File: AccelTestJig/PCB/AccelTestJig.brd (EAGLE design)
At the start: 10.2 x 24.1 mm, 11 parts, among them Q1 MMBTA56-SOT23, U1 MMA8653FCR1

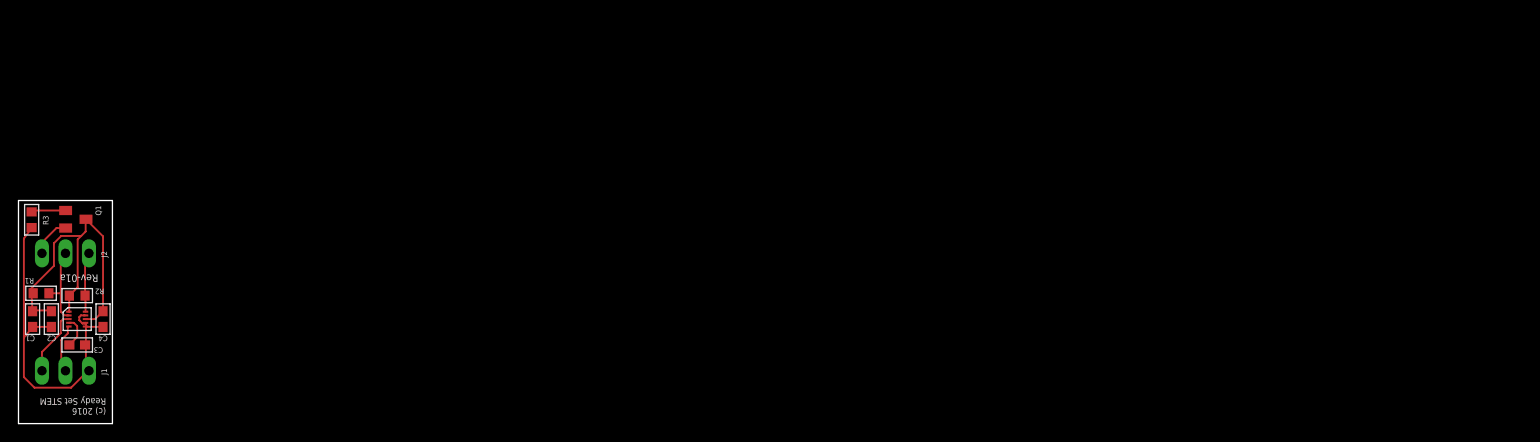
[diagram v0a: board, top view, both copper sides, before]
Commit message: AccelTestJig - first rev (sent to oshpark)
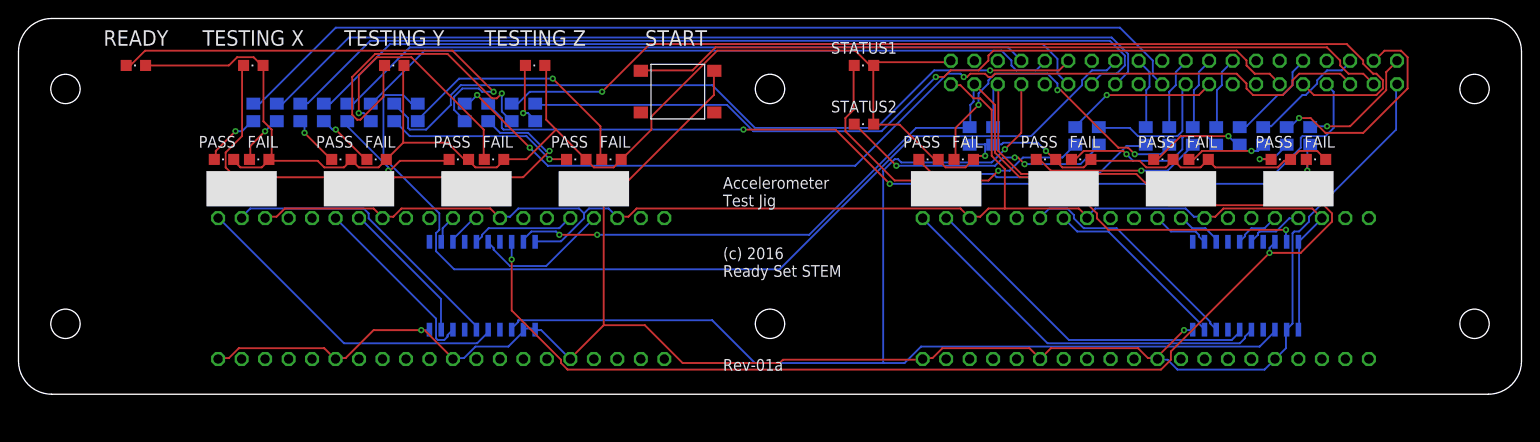
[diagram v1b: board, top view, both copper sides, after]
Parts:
- removed C1, C3, C4: 0.1uF, AccelBreakout:C0603
- removed C2: 1uF, AccelBreakout:C0603
- removed J1, J2: (no value), AccelBreakout:1X03
- removed Q1: MMBTA56-SOT23, transistor-pnp:SOT23
- added FAIL0, FAIL1, FAIL2, FAIL3, FAIL4, FAIL5, FAIL6, FAIL7: FAIL, led:CHIPLED_0805
- added JP1: NONE, AccelTestJig:2X20
- added JP2, JP3: NONE, AccelTestJig:2X20-WIDE
- added PASS0, PASS1, PASS2, PASS3, PASS4, PASS5, PASS6, PASS7: PASS, led:CHIPLED_0805
- added R10, R11, R12, R13, R14, R15, R16, R17, R18, R19, R20, R21, R22, R4, R5, R6, R7, R8, R9: 100, resistor:R0805
- added R23, R24: 10k, resistor:R0805
- added READY: READY, led:CHIPLED_0805
- added S1: START, AccelTestJig:6X6SMD
- added STATUS1, STATUS2: NONE, led:CHIPLED_0805
- added U2: NONE, AccelTestJig:SOIC20
- added XRUNNING: TESTING X, led:CHIPLED_0805
- added YRUNNING: TESTING Y, led:CHIPLED_0805
- added ZRUNNING: TESTING Z, led:CHIPLED_0805
- R1, R2, R3: value 10K -> 100; device AccelBreakout:R0603 -> resistor:R0805
- U1: value MMA8653FCR1 -> NONE; device AccelBreakout:MMA8653FCR1 -> AccelTestJig:SOIC20
- moved U1 49.5 mm to (55.9, 6.99), flipped to the bottom
- moved R3 43.3 mm to (43.2, 30.5), flipped to the bottom, turned to 270 degrees
- moved R1 38.5 mm to (35.6, 30.5), flipped to the bottom, turned to 270 degrees
- moved R2 37.4 mm to (38.1, 30.5), flipped to the bottom, turned to 270 degrees
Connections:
- removed net INT1: J1.1, U1.3
- removed net INT2: J1.2, U1.5
- removed net VCC: C1.1, C2.1, C4.1, Q1.3, R1.2, R2.2, U1.1, U1.8
- new net +3V3: JP1.1, JP2.16, JP2.26, JP2.36, JP2.6, JP3.16, JP3.26, JP3.36, JP3.6, U1.20, U2.1, U2.20
- new net +5V: FAIL0.A, FAIL1.A, FAIL2.A, FAIL3.A, FAIL4.A, FAIL5.A, FAIL6.A, FAIL7.A, JP1.2, PASS0.A, PASS1.A, PASS2.A, PASS3.A, PASS4.A, PASS5.A, PASS6.A, PASS7.A, R23.2, R24.2, READY.A, STATUS1.A, STATUS2.A, XRUNNING.A, YRUNNING.A, ZRUNNING.A
- new net N$13: FAIL7.C, R15.2
- new net N$14: FAIL1.C, R16.1
- new net N$15: PASS1.C, R17.1
- new net N$16: FAIL0.C, R18.1
- new net N$17: JP1.19, R19.2
- new net N$18: PASS0.C, R19.1
- new net N$19: JP1.8, R1.1
- new net N$20: JP1.10, R2.1
- new net N$21: JP1.12, R14.1
- new net N$22: PASS2.C, R1.2
- new net N$23: FAIL2.C, R2.2
- new net N$24: PASS3.C, R14.2
- new net N$25: FAIL3.C, R3.2
- new net N$26: PASS4.C, R4.2
- new net N$27: FAIL4.C, R5.2
- new net N$28: PASS5.C, R6.2
- new net N$29: FAIL5.C, R7.2
- new net N$3: JP1.15, R18.2
- new net N$30: PASS7.C, R10.2
- new net N$31: FAIL6.C, R9.2
- new net N$32: PASS6.C, R8.2
- new net N$33: JP1.16, R3.1
- new net N$35: JP1.22, R5.1
- new net N$36: JP1.24, R6.1
- new net N$37: JP1.26, R7.1
- new net N$38: JP1.32, R8.1
- new net N$39: JP1.36, R9.1
- new net N$40: JP1.38, R10.1
- new net N$41: JP1.40, R15.1
- new net N$42: R22.1, READY.C
- new net N$43: R21.1, XRUNNING.C
- new net N$44: R13.1, YRUNNING.C
- new net N$46: R11.1, STATUS1.C
- new net N$47: R20.1, STATUS2.C
- new net N$48: JP1.21, R20.2
- new net N$49: JP1.23, R11.2
- new net N$50: JP1.29, R12.2
- new net N$51: JP1.31, R13.2
- new net N$52: JP1.33, R21.2
- new net N$53: JP1.35, R22.2
- new net N$54: JP1.37, S1.P$1
- new net RESET#: JP1.7, U1.3, U2.3
- new net SC0: JP3.4, U2.6
- new net SC1: JP3.14, U2.9
- new net SC2: JP3.24, U2.13
- new net SC3: JP3.34, U2.16
- new net SC4: JP2.4, U1.6
- new net SC5: JP2.14, U1.9
- new net SC6: JP2.24, U1.13
- new net SC7: JP2.34, U1.16
- new net SD0: JP3.2, U2.5
- new net SD1: JP3.12, U2.8
- new net SD2: JP3.22, U2.12
- new net SD3: JP3.32, U2.15
- new net SD4: JP2.2, U1.5
- new net SD5: JP2.12, U1.8
- new net SD6: JP2.22, U1.12
- new net SD7: JP2.32, U1.15
- new net ZRUNNING: R12.1, ZRUNNING.C
- net GND: now also JP1.39, JP2.1, JP2.11, JP2.21, JP2.31, JP3.1, JP3.11, JP3.21, JP3.31, S1.P$2, U1.1, U1.10, U1.2, U2.10, U2.2; no longer C1.2, C2.2, C3.2, C4.2, J1.3, R3.1, U1.6, U1.7, U1.9
- net N$1: now also JP1.11, R16.2; no longer J2.1, Q1.2
- net N$2: now also JP1.13, R17.2; no longer Q1.1, R3.2
- net N$34: now also JP1.18, R4.1; no longer C3.1, U1.4
- net SCL: now also JP1.5, R23.1, U1.18, U2.18; no longer J2.2, R1.1, U1.2
- net SDA: now also JP1.3, R24.1, U1.19, U2.19; no longer J2.3, R2.1, U1.10
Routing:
- net +5V: track 0.00 -> 198.0 mm, vias 0 -> 2
- net GND: track 38.1 -> 201.5 mm, vias 0 -> 2
- net +3V3: track 0.00 -> 158.2 mm
- net SCL: track 8.84 -> 159.4 mm, vias 0 -> 2
- net RESET#: track 0.00 -> 129.8 mm, vias 0 -> 1
- net N$51: track 0.00 -> 109.1 mm, vias 0 -> 1
- net N$33: track 0.00 -> 107.5 mm
- net N$53: track 0.00 -> 107.1 mm, vias 0 -> 3
- net N$17: track 0.00 -> 105.2 mm
- net N$52: track 0.00 -> 103.9 mm, vias 0 -> 2
- net N$3: track 0.00 -> 99.6 mm
- net SDA: track 6.51 -> 103.6 mm, vias 0 -> 3
- net N$2: track 3.90 -> 98.2 mm
- net N$50: track 0.00 -> 87.5 mm, vias 0 -> 1
- net N$54: track 0.00 -> 82.3 mm
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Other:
- board size 10.2 x 24.1 mm -> 162.6 x 40.6 mm
- board text added: "Accelerometer Test Jig"
- board text added: "P"
- board text added: "READY"
- board text removed: "3.3V"
- board text removed: "GND"
- board text removed: "INT1"
- board text removed: "INT2"
- board text removed: "SCL"
- board text removed: "SDA"
